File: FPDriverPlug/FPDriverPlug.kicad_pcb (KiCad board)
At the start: 2 copper layers, 21 x 59.1 mm, 3 parts, among them CN1 Conn_02x05_Odd_Even, CN2 Conn_02x16_Counter_Clockwise, U1 FP2800A

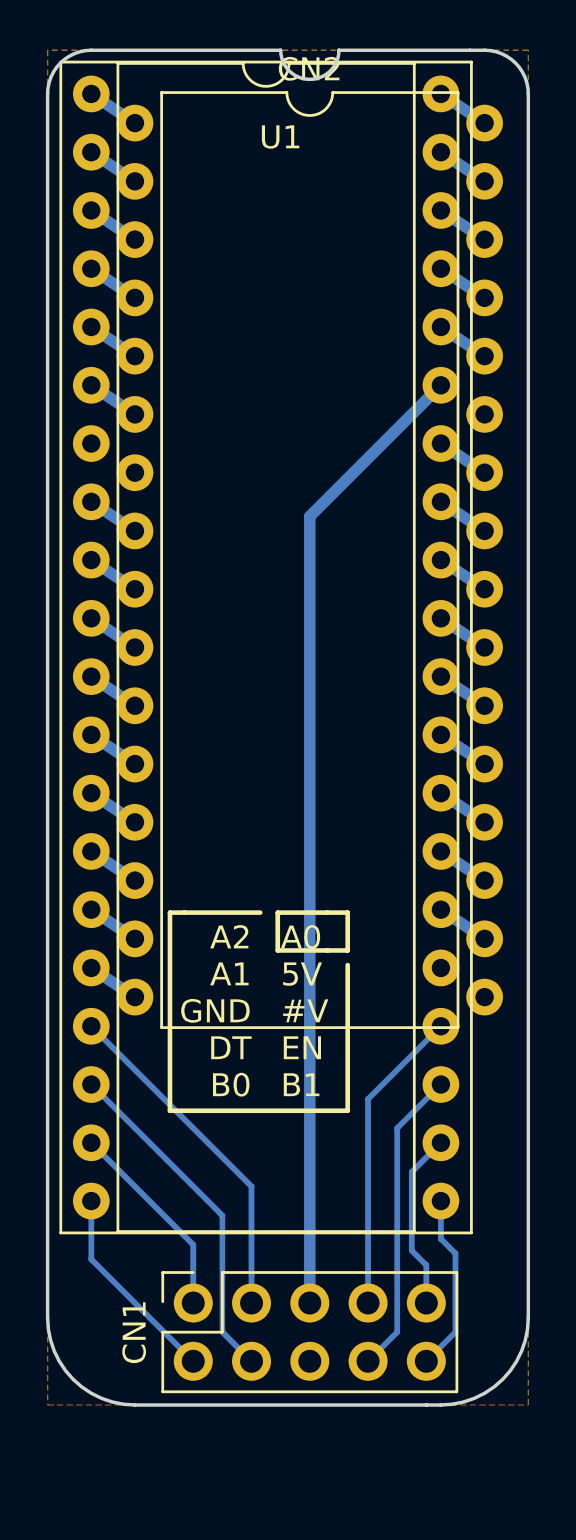
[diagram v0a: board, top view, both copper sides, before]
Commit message: adding rudimentary labeling on copper layers
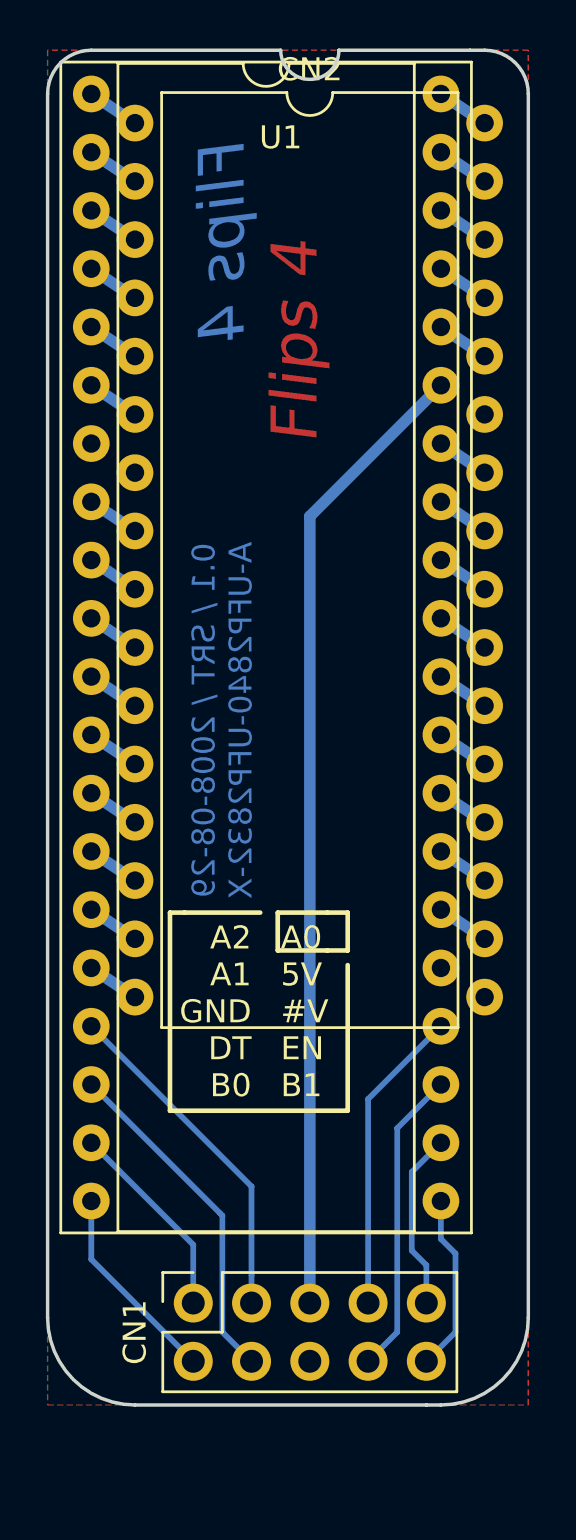
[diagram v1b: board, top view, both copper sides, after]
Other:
- board text added: "0.1 / SRT / 2008-08-29 A-UFP2840-UFP2832-X"
- board text added: "Flips 4"
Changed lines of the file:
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@@
   (general
     (thickness 1.6)
-    (drawings 29)
+    (drawings 32)
     (tracks 55)
     (zones 0)
@@
     )
   )
+  (gr_text "0.1 / SRT / 2008-08-29\nA-UFP2840-UFP2832-X" (at 226.06 93.98 90) (layer B.Cu)
+    (effects (font (size 1 1) (thickness 0.2)) (justify mirror))
+  )
+  (gr_text "Flips 4" (at 229.235 77.47 90) (layer F.Cu)
+    (effects (font (size 2 2) (thickness 0.5) italic))
+  )
+  (gr_text "Flips 4" (at 226.06 73.025 90) (layer B.Cu)
+    (effects (font (size 2 2) (thickness 0.5) italic) (justify mirror))
+  )
   (gr_text "A0\n5V\n#V\nEN\nB1" (at 228.6 106.68) (layer F.SilkS)

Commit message: 0.2 of Flips4
- Use IDC shrouded header
- Add more space between IC and header
- Center header
- Remove round corners
- Fix labels
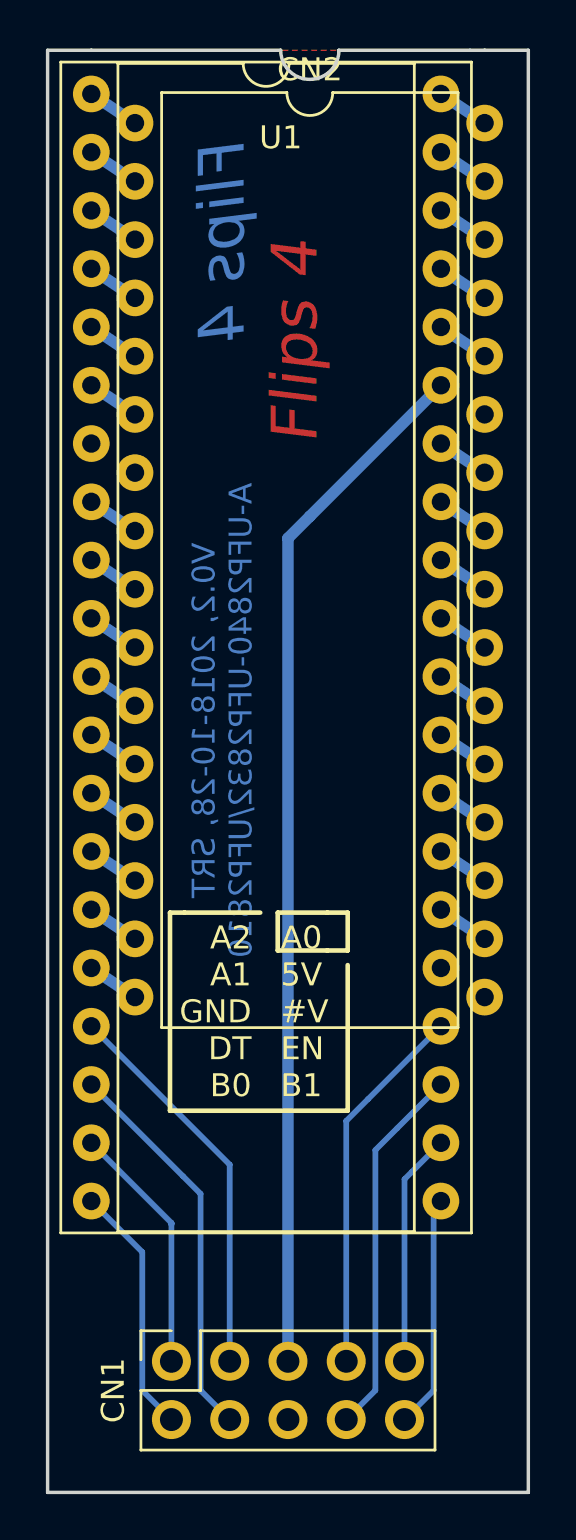
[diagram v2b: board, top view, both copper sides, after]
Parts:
- moved CN1 2.71 mm to (223.8, 121.9)
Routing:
- net +12V: track 42.4 -> 45.3 mm
- net /Enable: track 13.4 -> 16.3 mm
- net /Data: track 13.4 -> 16.3 mm
- net /B1: track 7.77 -> 10.2 mm
- net /B0: track 7.77 -> 10.2 mm
- net /A0: track 8.83 -> 11.1 mm
- net /A2: track 8.83 -> 11.0 mm
- net VCC: track 15.0 -> 17.1 mm
- net /A1: track 15.0 -> 17.1 mm
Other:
- board size 21 x 59.1 mm -> 21 x 62.9 mm
- board text added: "V0.2, 2018-10-28, SRT A-UFP2840-UFP2832/UFP2810"
- board text removed: "0.1 / SRT / 2008-08-29 A-UFP2840-UFP2832-X"

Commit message: shrinking Flips4 to minimum
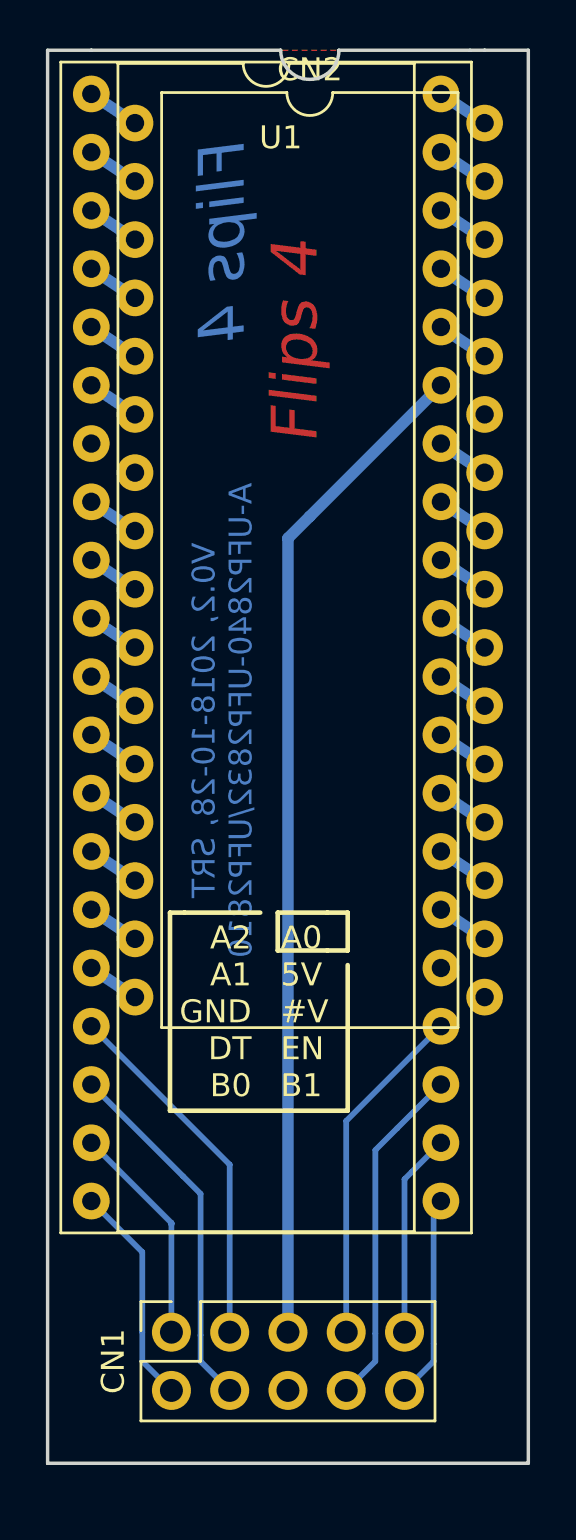
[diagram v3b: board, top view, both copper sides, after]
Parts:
- moved CN1 1.27 mm to (223.8, 120.7)
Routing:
- net /Enable: track 16.3 -> 15.0 mm
- net /Data: track 16.3 -> 15.0 mm
- net /B1: track 10.2 -> 8.91 mm
- net /B0: track 10.2 -> 8.91 mm
- net /A2: track 11.0 -> 9.70 mm
- net /A0: track 11.1 -> 9.83 mm
- net +12V: track 45.3 -> 44.0 mm
- net VCC: track 17.1 -> 15.8 mm
- net /A1: track 17.1 -> 15.8 mm
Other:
- board size 21 x 62.9 mm -> 21 x 61.6 mm
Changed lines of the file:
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@@
     (thickness 1.6)
     (drawings 29)
-    (tracks 58)
+    (tracks 61)
     (zones 0)
     (modules 3)
@@
   )
   (module Socket_Strips:Socket_Strip_Straight_2x05_Pitch2.54mm (layer F.Cu)
-    (at 223.8375 121.92 90)
+    (at 223.8375 120.65 90)
     (descr "Through hole straight socket strip, 2x05, 2.54mm pitch, double rows")
     (tags "Through hole socket strip THT 2x05 2.54mm double row")
@@
     )
   )
-  (dimension 62.865 (width 0.3) (layer Dwgs.User)
-    (gr_text "2,4750 in" (at 251.655 96.2025 90) (layer Dwgs.User)
+  (dimension 61.595 (width 0.3) (layer Dwgs.User)
+    (gr_text "2,4250 in" (at 251.655 95.5675 90) (layer Dwgs.User)
       (effects (font (size 1.5 1.5) (thickness 0.3)))
     )
     (feature1 (pts (xy 241.935 64.77) (xy 250.141421 64.77)))
-    (feature2 (pts (xy 241.935 127.635) (xy 250.141421 127.635)))
-    (crossbar (pts (xy 249.555 127.635) (xy 249.555 64.77)))
+    (feature2 (pts (xy 241.935 126.365) (xy 250.141421 126.365)))
+    (crossbar (pts (xy 249.555 126.365) (xy 249.555 64.77)))
     (arrow1a (pts (xy 249.555 64.77) (xy 250.141421 65.896504)))
     (arrow1b (pts (xy 249.555 64.77) (xy 248.968579 65.896504)))
-    (arrow2a (pts (xy 249.555 127.635) (xy 250.141421 126.508496)))
-    (arrow2b (pts (xy 249.555 127.635) (xy 248.968579 126.508496)))
-  )
-  (dimension 62.865 (width 0.3) (layer Dwgs.User)
-    (gr_text "62,865 mm" (at 197.925 96.2025 90) (layer Dwgs.User)
+    (arrow2a (pts (xy 249.555 126.365) (xy 250.141421 125.238496)))
+    (arrow2b (pts (xy 249.555 126.365) (xy 248.968579 125.238496)))
+  )
+  (dimension 61.595 (width 0.3) (layer Dwgs.User)
+    (gr_text "61,595 mm" (at 197.925 95.5675 90) (layer Dwgs.User)
       (effects (font (size 1.5 1.5) (thickness 0.3)))
     )
     (feature1 (pts (xy 209.55 64.77) (xy 199.438579 64.77)))
-    (feature2 (pts (xy 209.55 127.635) (xy 199.438579 127.635)))
-    (crossbar (pts (xy 200.025 127.635) (xy 200.025 64.77)))
+    (feature2 (pts (xy 209.55 126.365) (xy 199.438579 126.365)))
+    (crossbar (pts (xy 200.025 126.365) (xy 200.025 64.77)))
     (arrow1a (pts (xy 200.025 64.77) (xy 200.611421 65.896504)))
     (arrow1b (pts (xy 200.025 64.77) (xy 199.438579 65.896504)))
-    (arrow2a (pts (xy 200.025 127.635) (xy 200.611421 126.508496)))
-    (arrow2b (pts (xy 200.025 127.635) (xy 199.438579 126.508496)))
-  )
-  (gr_line (start 218.44 127.635) (end 218.44 64.77) (angle 90) (layer Edge.Cuts) (width 0.15))
-  (gr_line (start 239.395 64.77) (end 239.395 127.635) (angle 90) (layer Edge.Cuts) (width 0.15))
-  (gr_line (start 218.44 127.635) (end 239.395 127.635) (angle 90) (layer Edge.Cuts) (width 0.15))
+    (arrow2a (pts (xy 200.025 126.365) (xy 200.611421 125.238496)))
+    (arrow2b (pts (xy 200.025 126.365) (xy 199.438579 125.238496)))
+  )
+  (gr_line (start 218.44 64.77) (end 218.44 126.365) (angle 90) (layer Edge.Cuts) (width 0.15))
+  (gr_line (start 239.395 126.365) (end 239.395 64.77) (angle 90) (layer Edge.Cuts) (width 0.15))
+  (gr_line (start 218.44 126.365) (end 239.395 126.365) (angle 90) (layer Edge.Cuts) (width 0.15))
   (gr_line (start 239.395 64.77) (end 237.49 64.77) (angle 90) (layer Edge.Cuts) (width 0.15))
   (gr_line (start 218.44 64.77) (end 220.345 64.77) (angle 90) (layer Edge.Cuts) (width 0.15))
@@
   (segment (start 220.345 66.675) (end 222.25 67.945) (width 0.5) (layer B.Cu) (net 32) (status C00000))
   (segment (start 226.3775 113.3475) (end 220.345 107.315) (width 0.25) (layer B.Cu) (net 34) (status 800000))
-  (segment (start 226.3775 121.92) (end 226.3775 113.3475) (width 0.25) (layer B.Cu) (net 34) (status 400000))
-  (segment (start 235.585 79.375) (end 229.87 85.09) (width 0.5) (layer B.Cu) (net 35))
-  (segment (start 228.9175 121.92) (end 228.9175 86.0425) (width 0.5) (layer B.Cu) (net 35) (status 400000))
+  (segment (start 226.3775 120.65) (end 226.3775 113.3475) (width 0.25) (layer B.Cu) (net 34))
+  (segment (start 229.87 85.09) (end 235.585 79.375) (width 0.5) (layer B.Cu) (net 35))
+  (segment (start 228.9175 120.65) (end 228.9175 86.0425) (width 0.5) (layer B.Cu) (net 35))
   (segment (start 228.9175 86.0425) (end 229.87 85.09) (width 0.5) (layer B.Cu) (net 35))
-  (segment (start 233.9975 124.46) (end 235.2675 123.19) (width 0.25) (layer B.Cu) (net 36) (status 400000))
   (segment (start 235.2675 115.2525) (end 235.585 114.935) (width 0.25) (layer B.Cu) (net 36) (status C00000))
-  (segment (start 235.2675 123.19) (end 235.2675 115.2525) (width 0.25) (layer B.Cu) (net 36) (status 800000))
+  (segment (start 235.2675 121.92) (end 233.9975 123.19) (width 0.25) (layer B.Cu) (net 36))
+  (segment (start 235.2675 121.158) (end 235.2675 121.92) (width 0.25) (layer B.Cu) (net 36))
+  (segment (start 235.2675 121.158) (end 235.2675 115.2525) (width 0.25) (layer B.Cu) (net 36))
   (segment (start 235.585 112.395) (end 234.315 113.665) (width 0.25) (layer B.Cu) (net 37))
-  (segment (start 233.9975 121.92) (end 233.9975 113.9825) (width 0.25) (layer B.Cu) (net 37) (status 400000))
   (segment (start 233.9975 113.9825) (end 234.315 113.665) (width 0.25) (layer B.Cu) (net 37))
+  (segment (start 233.9975 120.65) (end 233.9975 113.9825) (width 0.25) (layer B.Cu) (net 37))
   (segment (start 235.585 109.855) (end 233.68 111.76) (width 0.25) (layer B.Cu) (net 38) (status 400000))
-  (segment (start 231.4575 124.46) (end 232.7275 123.19) (width 0.25) (layer B.Cu) (net 38) (status 400000))
   (segment (start 232.7275 112.7125) (end 233.68 111.76) (width 0.25) (layer B.Cu) (net 38))
-  (segment (start 232.7275 123.19) (end 232.7275 112.7125) (width 0.25) (layer B.Cu) (net 38))
-  (segment (start 235.585 107.315) (end 232.41 110.49) (width 0.25) (layer B.Cu) (net 39))
-  (segment (start 231.4575 121.92) (end 231.4575 111.4425) (width 0.25) (layer B.Cu) (net 39) (status 400000))
-  (segment (start 231.4575 111.4425) (end 232.41 110.49) (width 0.25) (layer B.Cu) (net 39))
+  (segment (start 232.7275 121.92) (end 231.4575 123.19) (width 0.25) (layer B.Cu) (net 38))
+  (segment (start 232.7275 120.7135) (end 232.7275 121.92) (width 0.25) (layer B.Cu) (net 38))
+  (segment (start 232.7275 120.7135) (end 232.7275 112.7125) (width 0.25) (layer B.Cu) (net 38))
+  (segment (start 231.4575 111.4425) (end 231.4575 120.65) (width 0.25) (layer B.Cu) (net 39))
+  (segment (start 235.585 107.315) (end 231.4575 111.4425) (width 0.25) (layer B.Cu) (net 39))
   (segment (start 220.345 109.855) (end 224.3455 113.8555) (width 0.25) (layer B.Cu) (net 40) (status 400000))
-  (segment (start 226.3775 124.46) (end 225.1075 123.19) (width 0.25) (layer B.Cu) (net 40) (status 400000))
   (segment (start 225.1075 114.6175) (end 224.3455 113.8555) (width 0.25) (layer B.Cu) (net 40))
-  (segment (start 225.1075 123.19) (end 225.1075 114.6175) (width 0.25) (layer B.Cu) (net 40))
-  (segment (start 223.8375 124.46) (end 222.5675 123.19) (width 0.25) (layer B.Cu) (net 41) (status 400000))
+  (segment (start 225.1075 121.92) (end 226.3775 123.19) (width 0.25) (layer B.Cu) (net 40))
+  (segment (start 225.1075 120.777) (end 225.1075 121.92) (width 0.25) (layer B.Cu) (net 40))
+  (segment (start 225.1075 120.777) (end 225.1075 114.6175) (width 0.25) (layer B.Cu) (net 40))
   (segment (start 222.5675 117.1575) (end 220.345 114.935) (width 0.25) (layer B.Cu) (net 41) (status 800000))
-  (segment (start 222.5675 123.19) (end 222.5675 117.1575) (width 0.25) (layer B.Cu) (net 41))
+  (segment (start 222.5675 121.92) (end 223.8375 123.19) (width 0.25) (layer B.Cu) (net 41))
+  (segment (start 222.5675 120.65) (end 222.5675 121.92) (width 0.25) (layer B.Cu) (net 41))
+  (segment (start 222.5675 120.65) (end 222.5675 117.1575) (width 0.25) (layer B.Cu) (net 41))
   (segment (start 223.8375 115.8875) (end 220.345 112.395) (width 0.25) (layer B.Cu) (net 42) (status 800000))
-  (segment (start 223.8375 121.92) (end 223.8375 115.8875) (width 0.25) (layer B.Cu) (net 42) (status 400000))
   (segment (start 223.8375 115.8875) (end 223.8375 115.951) (width 0.25) (layer B.Cu) (net 42))
   (segment (start 223.8375 115.951) (end 223.8375 115.8875) (width 0.25) (layer B.Cu) (net 42))
+  (segment (start 223.8375 120.65) (end 223.8375 115.8875) (width 0.25) (layer B.Cu) (net 42))
   (zone (net 33) (net_name GND) (layer F.Cu) (hatch edge 0.508)
     (connect_pads (clearance 0.1524))
@@
     (polygon
       (pts
-        (xy 218.44 127.635) (xy 239.395 127.635) (xy 239.395 64.77) (xy 218.44 64.77)
+        (xy 218.44 126.365) (xy 239.395 126.365) (xy 239.395 64.77) (xy 218.44 64.77)
       )
     )

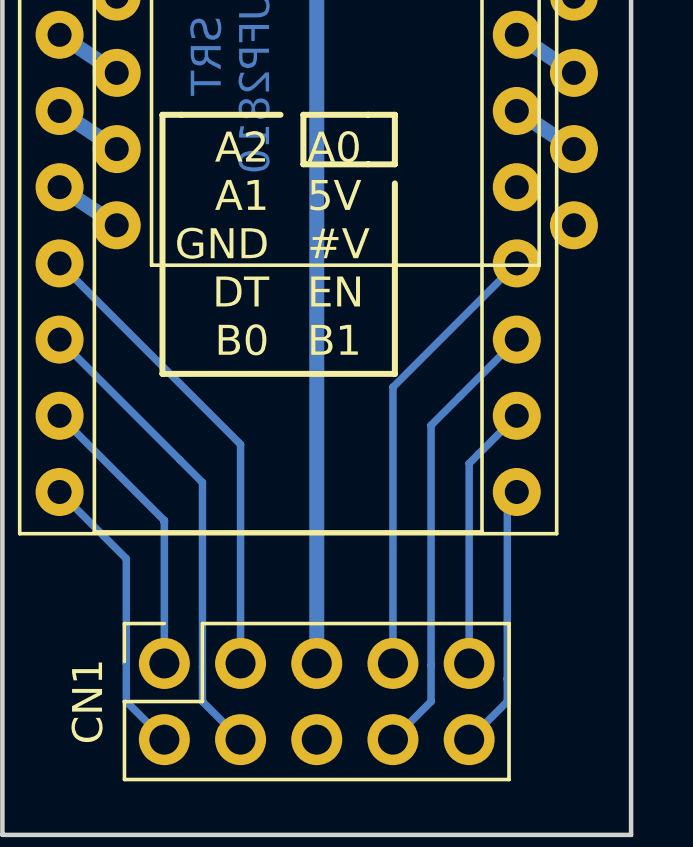
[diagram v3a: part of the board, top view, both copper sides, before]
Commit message: adding optional pulldown for ENABLE
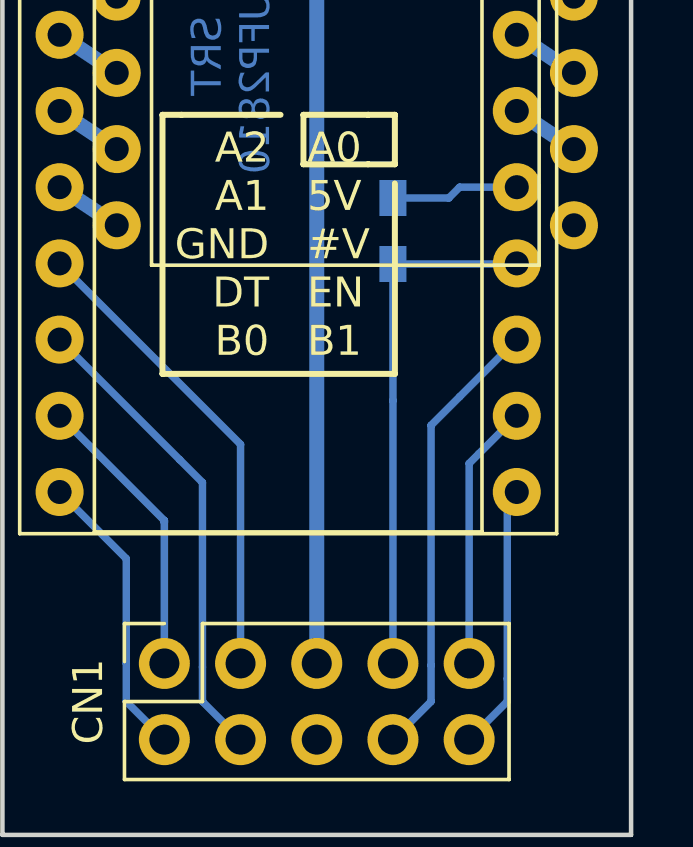
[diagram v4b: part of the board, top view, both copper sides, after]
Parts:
- added R1: 10K/OPT, Resistors_SMD:R_0603_HandSoldering, B.Cu at (231.5, 106.2)
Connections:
- CN2 pad 17: Net-(CN2-Pad17) -> (no net)
- CN2 pad 27: Net-(CN2-Pad27) -> (no net)
- CN2 pad 7: Net-(CN2-Pad7) -> (no net)
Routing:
- net GND: track 0.00 -> 4.28 mm
- net /Enable: track 15.0 -> 17.5 mm
